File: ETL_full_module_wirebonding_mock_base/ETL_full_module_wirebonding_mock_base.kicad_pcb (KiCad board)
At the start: 2 copper layers, 56.5 x 43.1 mm, 12 parts

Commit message: Updates ETL_full_module_wirebonding_mock_base and top
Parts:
- moved ETROC** 0.40 mm to (3.05, 6.25)
- moved ETROC** 0.40 mm to (3.05, 36.9)
- moved ETROC** 0.40 mm to (53.9, 36.9)
- moved ETROC** 0.40 mm to (53.9, 6.25)
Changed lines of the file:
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@@
   (general
     (thickness 1.6)
-    (drawings 12)
+    (drawings 13)
     (tracks 0)
     (zones 0)
@@
     (pad_to_mask_clearance 0.05)
     (aux_axis_origin 0 0)
-    (visible_elements FFFFFF7F)
+    (visible_elements 7FFFFFFF)
     (pcbplotparams
-      (layerselection 0x010fc_ffffffff)
+      (layerselection 0x010a8_7fffffff)
       (usegerberextensions false)
       (usegerberattributes true)
@@
       (outputformat 1)
       (mirror false)
-      (drillshape 1)
+      (drillshape 0)
       (scaleselection 1)
-      (outputdirectory ""))
+      (outputdirectory "fab_outputs/"))
   )
   (net 0 "")
@@
       (effects (font (size 1 1) (thickness 0.15)))
     )
+    (fp_circle (center 0 0) (end 0.01 0) (layer F.Mask) (width 0.6))
+    (fp_line (start 0.25 0) (end -0.25 0) (layer F.Cu) (width 0.07))
+    (fp_line (start 0 -0.25) (end 0 0.25) (layer F.Cu) (width 0.07))
     (fp_circle (center 0 0) (end 0.2 0) (layer F.Cu) (width 0.07))
-    (fp_line (start 0 -0.25) (end 0 0.25) (layer F.Cu) (width 0.07))
-    (fp_line (start 0.25 0) (end -0.25 0) (layer F.Cu) (width 0.07))
-    (fp_circle (center 0 0) (end 0.01 0) (layer F.Mask) (width 0.6))
   )
   (module unl_silab:crossed_circle_fiducial (layer F.Cu)
@@
       (effects (font (size 1 1) (thickness 0.15)))
     )
+    (fp_circle (center 0 0) (end 0.01 0) (layer F.Mask) (width 0.6))
+    (fp_line (start 0.25 0) (end -0.25 0) (layer F.Cu) (width 0.07))
+    (fp_line (start 0 -0.25) (end 0 0.25) (layer F.Cu) (width 0.07))
     (fp_circle (center 0 0) (end 0.2 0) (layer F.Cu) (width 0.07))
-    (fp_line (start 0 -0.25) (end 0 0.25) (layer F.Cu) (width 0.07))
-    (fp_line (start 0.25 0) (end -0.25 0) (layer F.Cu) (width 0.07))
-    (fp_circle (center 0 0) (end 0.01 0) (layer F.Mask) (width 0.6))
   )
   (module unl_silab:crossed_circle_fiducial (layer F.Cu)
@@
       (effects (font (size 1 1) (thickness 0.15)))
     )
+    (fp_circle (center 0 0) (end 0.01 0) (layer F.Mask) (width 0.6))
+    (fp_line (start 0.25 0) (end -0.25 0) (layer F.Cu) (width 0.07))
+    (fp_line (start 0 -0.25) (end 0 0.25) (layer F.Cu) (width 0.07))
     (fp_circle (center 0 0) (end 0.2 0) (layer F.Cu) (width 0.07))
-    (fp_line (start 0 -0.25) (end 0 0.25) (layer F.Cu) (width 0.07))
-    (fp_line (start 0.25 0) (end -0.25 0) (layer F.Cu) (width 0.07))
-    (fp_circle (center 0 0) (end 0.01 0) (layer F.Mask) (width 0.6))
   )
   (module MountingHole:MountingHole_2.5mm (layer F.Cu)
@@
       (effects (font (size 1 1) (thickness 0.15)))
     )
+    (fp_circle (center 0 0) (end 2.75 0) (layer F.CrtYd) (width 0.05))
     (fp_circle (center 0 0) (end 2.5 0) (layer Cmts.User) (width 0.15))
-    (fp_circle (center 0 0) (end 2.75 0) (layer F.CrtYd) (width 0.05))
     (fp_text user %R (at 0.3 0) (layer F.Fab)
       (effects (font (size 1 1) (thickness 0.15)))
@@
       (effects (font (size 1 1) (thickness 0.15)))
     )
+    (fp_circle (center 0 0) (end 2.75 0) (layer F.CrtYd) (width 0.05))
     (fp_circle (center 0 0) (end 2.5 0) (layer Cmts.User) (width 0.15))
-    (fp_circle (center 0 0) (end 2.75 0) (layer F.CrtYd) (width 0.05))
     (fp_text user %R (at 0.3 0) (layer F.Fab)
       (effects (font (size 1 1) (thickness 0.15)))
@@
       (effects (font (size 1 1) (thickness 0.15)))
     )
+    (fp_circle (center 0 0) (end 2.75 0) (layer F.CrtYd) (width 0.05))
     (fp_circle (center 0 0) (end 2.5 0) (layer Cmts.User) (width 0.15))
-    (fp_circle (center 0 0) (end 2.75 0) (layer F.CrtYd) (width 0.05))
     (fp_text user %R (at 0.3 0) (layer F.Fab)
       (effects (font (size 1 1) (thickness 0.15)))
@@
       (effects (font (size 1 1) (thickness 0.15)))
     )
+    (fp_circle (center 0 0) (end 2.75 0) (layer F.CrtYd) (width 0.05))
+    (fp_circle (center 0 0) (end 2.5 0) (layer Cmts.User) (width 0.15))
     (fp_text user %R (at 0.3 0) (layer F.Fab)
       (effects (font (size 1 1) (thickness 0.15)))
     )
-    (fp_circle (center 0 0) (end 2.5 0) (layer Cmts.User) (width 0.15))
-    (fp_circle (center 0 0) (end 2.75 0) (layer F.CrtYd) (width 0.05))
     (pad 1 np_thru_hole circle (at 0 0) (size 2.5 2.5) (drill 2.5) (layers *.Cu *.Mask))
   )
@@
       (effects (font (size 1 1) (thickness 0.15)))
     )
+    (fp_circle (center 0 0) (end 0.01 0) (layer F.Mask) (width 0.6))
+    (fp_line (start 0.25 0) (end -0.25 0) (layer F.Cu) (width 0.07))
+    (fp_line (start 0 -0.25) (end 0 0.25) (layer F.Cu) (width 0.07))
     (fp_circle (center 0 0) (end 0.2 0) (layer F.Cu) (width 0.07))
-    (fp_line (start 0 -0.25) (end 0 0.25) (layer F.Cu) (width 0.07))
-    (fp_line (start 0.25 0) (end -0.25 0) (layer F.Cu) (width 0.07))
-    (fp_circle (center 0 0) (end 0.01 0) (layer F.Mask) (width 0.6))
   )
   (module unl_silab:ETROC_70pad_100x150um_200um_pitch (layer F.Cu)
-    (at 53.5 36.85 90)
+    (at 53.9 36.85 90)
     (fp_text reference ETROC** (at 0 0.5 90) (layer F.SilkS) hide
       (effects (font (size 1 1) (thickness 0.15)))
@@
   )
   (module unl_silab:ETROC_70pad_100x150um_200um_pitch (layer F.Cu)
-    (at 53.5 6.25 270)
+    (at 53.9 6.25 270)
     (fp_text reference ETROC** (at 0 0.5 90) (layer F.SilkS) hide
       (effects (font (size 1 1) (thickness 0.15)))
@@
   )
   (module unl_silab:ETROC_70pad_100x150um_200um_pitch (layer F.Cu)
-    (at 3.45 6.25 270)
+    (at 3.05 6.25 270)
     (fp_text reference ETROC** (at 0 0.5 90) (layer F.SilkS) hide
       (effects (font (size 1 1) (thickness 0.15)))
@@
   )
   (module unl_silab:ETROC_70pad_100x150um_200um_pitch (layer F.Cu)
-    (at 3.45 36.85 90)
+    (at 3.05 36.85 90)
     (fp_text reference ETROC** (at 0 0.5 90) (layer F.SilkS) hide
       (effects (font (size 1 1) (thickness 0.15)))
@@
     (pad 1 smd rect (at 0 0 90) (size 0.1 0.15) (layers F.Cu F.Mask))
   )
-  (dimension 40.850001 (width 0.15) (layer Dwgs.User)
-    (gr_text "40.850 mm" (at 48.95 22.424999 90) (layer Dwgs.User)
-      (effects (font (size 1 1) (thickness 0.15)))
-    )
-    (feature1 (pts (xy 52.05 1.999999) (xy 49.663579 1.999999)))
-    (feature2 (pts (xy 52.05 42.85) (xy 49.663579 42.85)))
-    (crossbar (pts (xy 50.25 42.85) (xy 50.25 1.999999)))
-    (arrow1a (pts (xy 50.25 1.999999) (xy 50.836421 3.126503)))
-    (arrow1b (pts (xy 50.25 1.999999) (xy 49.663579 3.126503)))
-    (arrow2a (pts (xy 50.25 42.85) (xy 50.836421 41.723496)))
-    (arrow2b (pts (xy 50.25 42.85) (xy 49.663579 41.723496)))
-  )
   (dimension 47.6 (width 0.15) (layer Dwgs.User)
-    (gr_text "47.600 mm" (at 28.25 3.299999) (layer Dwgs.User)
-      (effects (font (size 1 1) (thickness 0.15)))
-    )
-    (feature1 (pts (xy 52.05 0.25) (xy 52.05 2.58642)))
-    (feature2 (pts (xy 4.45 0.25) (xy 4.45 2.58642)))
-    (crossbar (pts (xy 4.45 1.999999) (xy 52.05 1.999999)))
-    (arrow1a (pts (xy 52.05 1.999999) (xy 50.923496 2.58642)))
-    (arrow1b (pts (xy 52.05 1.999999) (xy 50.923496 1.413578)))
-    (arrow2a (pts (xy 4.45 1.999999) (xy 5.576504 2.58642)))
-    (arrow2b (pts (xy 4.45 1.999999) (xy 5.576504 1.413578)))
+    (gr_text "47.600 mm" (at 28.25 2.95) (layer Dwgs.User)
+      (effects (font (size 1 1) (thickness 0.15)))
+    )
+    (feature1 (pts (xy 4.45 0.7) (xy 4.45 2.236421)))
+    (feature2 (pts (xy 52.05 0.7) (xy 52.05 2.236421)))
+    (crossbar (pts (xy 52.05 1.65) (xy 4.45 1.65)))
+    (arrow1a (pts (xy 4.45 1.65) (xy 5.576504 1.063579)))
+    (arrow1b (pts (xy 4.45 1.65) (xy 5.576504 2.236421)))
+    (arrow2a (pts (xy 52.05 1.65) (xy 50.923496 1.063579)))
+    (arrow2b (pts (xy 52.05 1.65) (xy 50.923496 2.236421)))
+  )
+  (dimension 41.7 (width 0.15) (layer Dwgs.User)
+    (gr_text "41.700 mm" (at 48.3 21.55 90) (layer Dwgs.User)
+      (effects (font (size 1 1) (thickness 0.15)))
+    )
+    (feature1 (pts (xy 52.05 0.7) (xy 49.013579 0.7)))
+    (feature2 (pts (xy 52.05 42.4) (xy 49.013579 42.4)))
+    (crossbar (pts (xy 49.6 42.4) (xy 49.6 0.7)))
+    (arrow1a (pts (xy 49.6 0.7) (xy 50.186421 1.826504)))
+    (arrow1b (pts (xy 49.6 0.7) (xy 49.013579 1.826504)))
+    (arrow2a (pts (xy 49.6 42.4) (xy 50.186421 41.273496)))
+    (arrow2b (pts (xy 49.6 42.4) (xy 49.013579 41.273496)))
+  )
+  (dimension 1.85 (width 0.15) (layer Dwgs.User)
+    (gr_text "1.850 mm" (at 52.975 -6.7) (layer Dwgs.User)
+      (effects (font (size 1 1) (thickness 0.15)))
+    )
+    (feature1 (pts (xy 52.05 6.25) (xy 52.05 -5.986421)))
+    (feature2 (pts (xy 53.9 6.25) (xy 53.9 -5.986421)))
+    (crossbar (pts (xy 53.9 -5.4) (xy 52.05 -5.4)))
+    (arrow1a (pts (xy 52.05 -5.4) (xy 53.176504 -5.986421)))
+    (arrow1b (pts (xy 52.05 -5.4) (xy 53.176504 -4.813579)))
+    (arrow2a (pts (xy 53.9 -5.4) (xy 52.773496 -5.986421)))
+    (arrow2b (pts (xy 53.9 -5.4) (xy 52.773496 -4.813579)))
   )
   (dimension 43.1 (width 0.15) (layer Dwgs.User)
@@
     (arrow2b (pts (xy 56.5 -1.749999) (xy 55.373496 -1.163578)))
   )
-  (gr_line (start 4.45 0.25) (end 52.05 0.25) (layer F.SilkS) (width 0.15))
-  (gr_line (start 52.05 0.25) (end 52.05 42.85) (layer F.SilkS) (width 0.15))
-  (gr_line (start 4.45 42.85) (end 52.05 42.85) (layer F.SilkS) (width 0.15))
-  (gr_line (start 4.45 0.25) (end 4.45 42.85) (layer F.SilkS) (width 0.15))
+  (gr_line (start 4.45 0.7) (end 52.05 0.7) (layer F.SilkS) (width 0.15))
+  (gr_line (start 52.05 0.7) (end 52.05 42.4) (layer F.SilkS) (width 0.15))
+  (gr_line (start 4.45 42.4) (end 52.05 42.4) (layer F.SilkS) (width 0.15))
+  (gr_line (start 4.45 0.7) (end 4.45 42.4) (layer F.SilkS) (width 0.15))
   (gr_line (start 0 0) (end 56.5 0) (layer Edge.Cuts) (width 0.05))
   (gr_line (start 56.5 0) (end 56.5 43.1) (layer Edge.Cuts) (width 0.05))

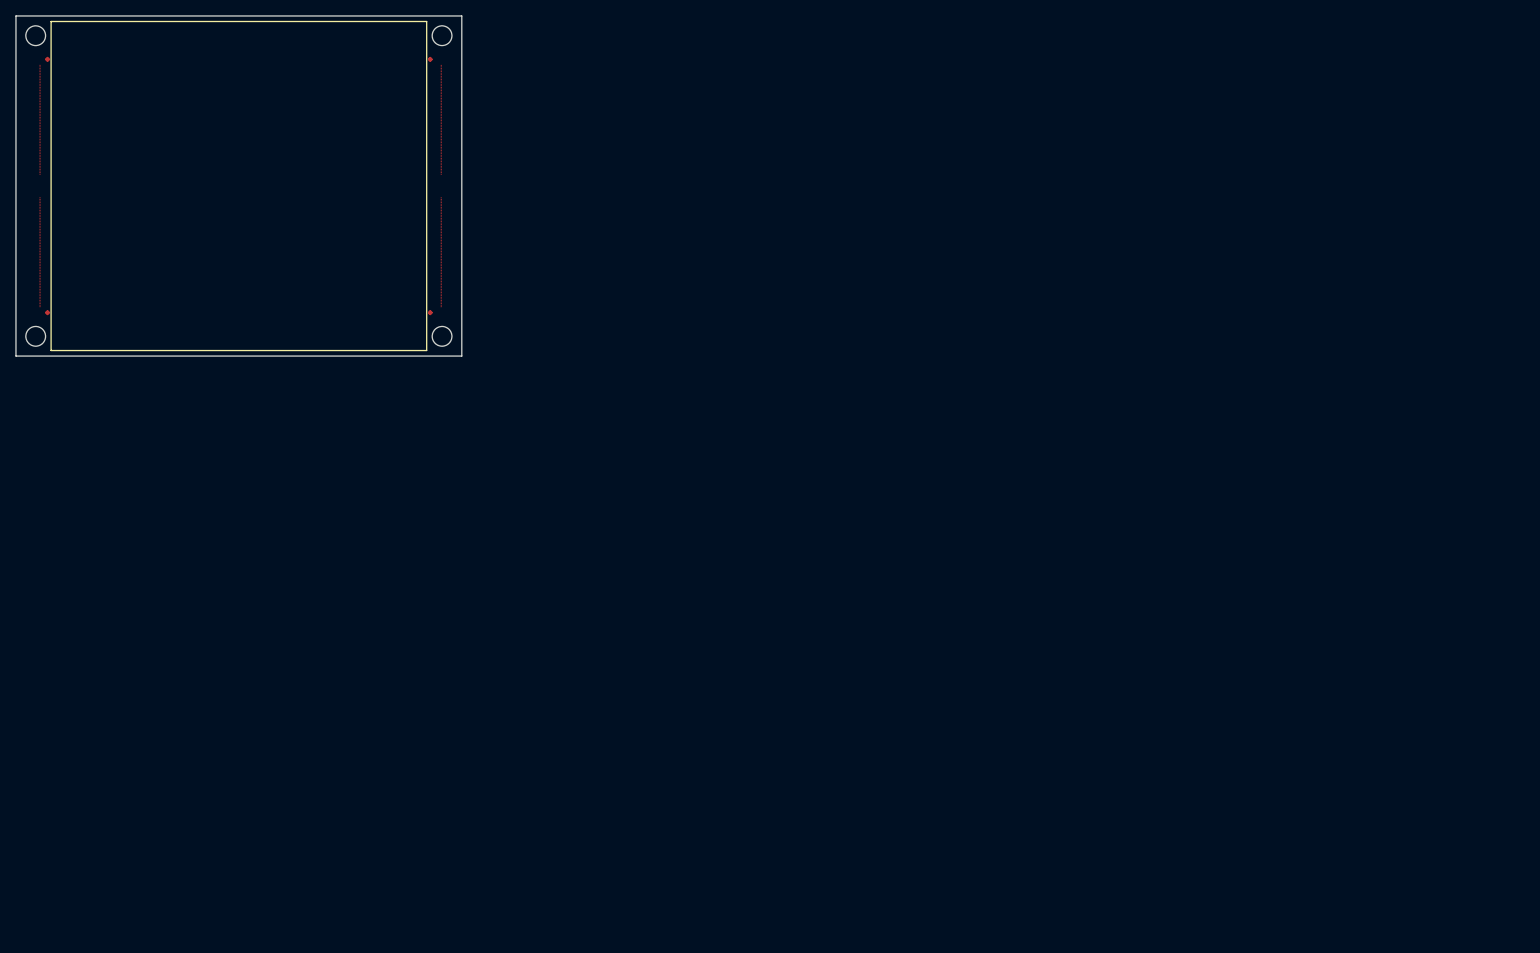
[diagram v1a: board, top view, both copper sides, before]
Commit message: Fixes hole placement in ETL_full_module_wirebonding_mock_base
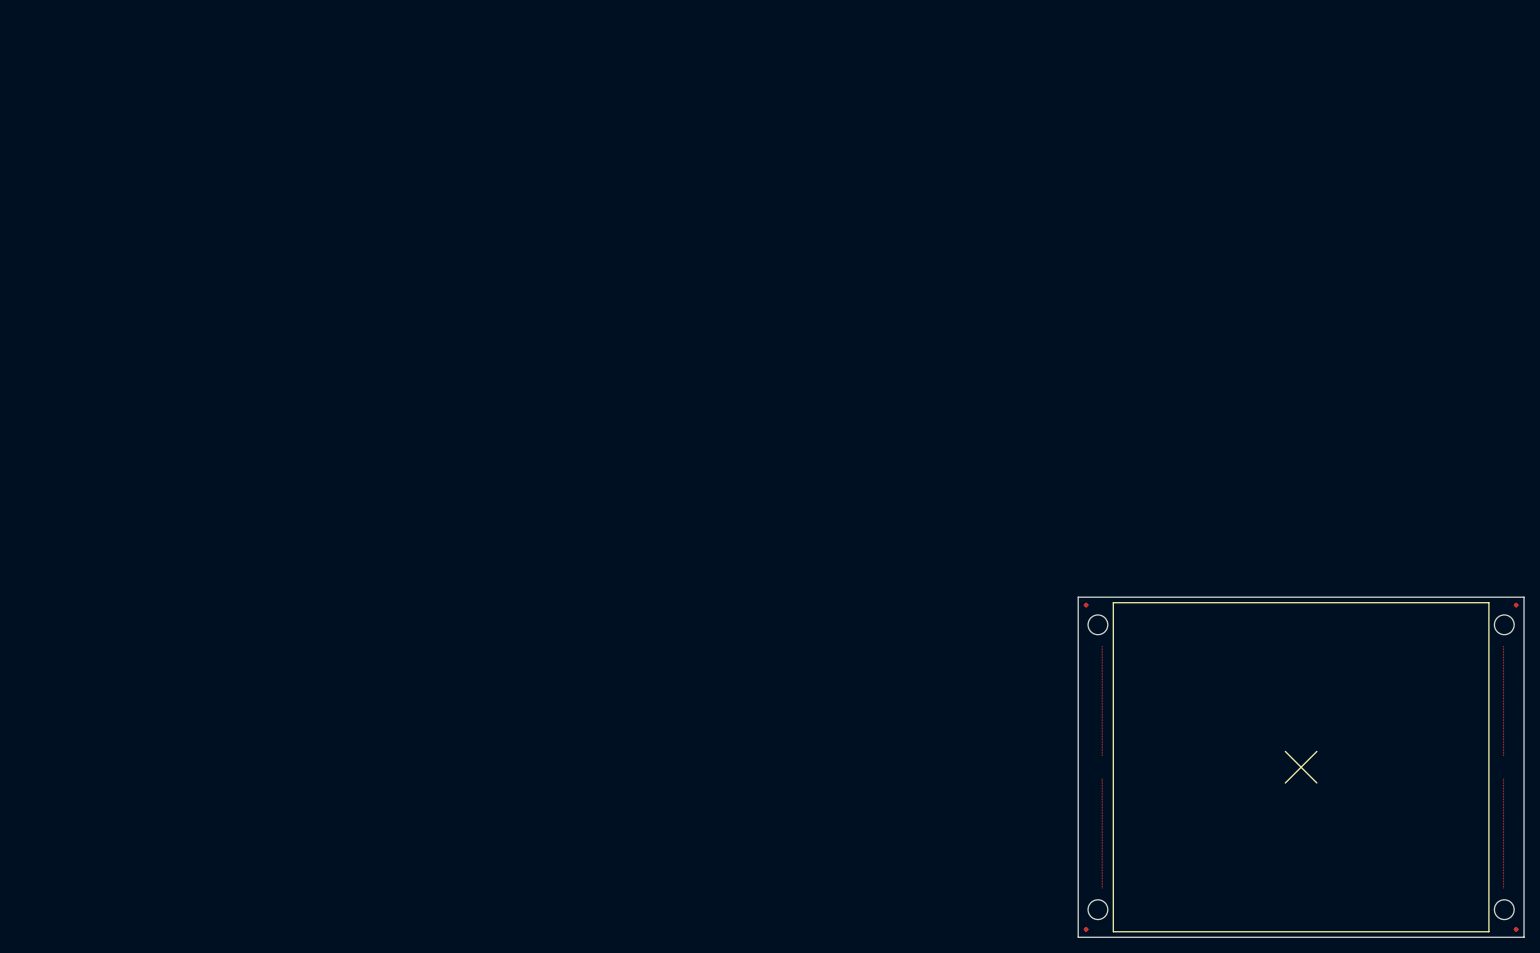
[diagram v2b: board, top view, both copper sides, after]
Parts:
- removed the REF** at (52.5, 37.6)
- removed the REF** at (4.00, 37.6)
- removed the REF** at (54.0, 2.50)
- removed the REF** at (54.0, 40.6)
- removed the REF** at (2.50, 40.6)
- added REF**: crossed_circle_fiducial, unl_silab:crossed_circle_fiducial, F.Cu at (190.1, 115.8)
- added REF**: crossed_circle_fiducial, unl_silab:crossed_circle_fiducial, F.Cu at (135.6, 115.8)
- added REF**: MountingHole_2.5mm, MountingHole:MountingHole_2.5mm, F.Cu at (188.6, 77.2)
- added REF**: MountingHole_2.5mm, MountingHole:MountingHole_2.5mm, F.Cu at (188.6, 113.3)
- added REF**: MountingHole_2.5mm, MountingHole:MountingHole_2.5mm, F.Cu at (137.1, 113.3)
- moved REF** 154.0 mm to (190.1, 74.7)
- moved REF** 153.9 mm to (137.1, 77.2)
- moved ETROC** 153.5 mm to (188.5, 110.5)
- moved ETROC** 153.5 mm to (188.5, 79.9)
- moved ETROC** 153.5 mm to (137.7, 79.9)
- moved ETROC** 153.5 mm to (137.7, 110.5)
- moved REF** 148.7 mm to (135.6, 74.7)
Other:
- rule pad_to_mask_clearance: 0.05 -> 0
